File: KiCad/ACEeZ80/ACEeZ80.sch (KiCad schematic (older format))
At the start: 37 parts, among them J1 Connector_Generic:Conn_02x20_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, X2 50MHz

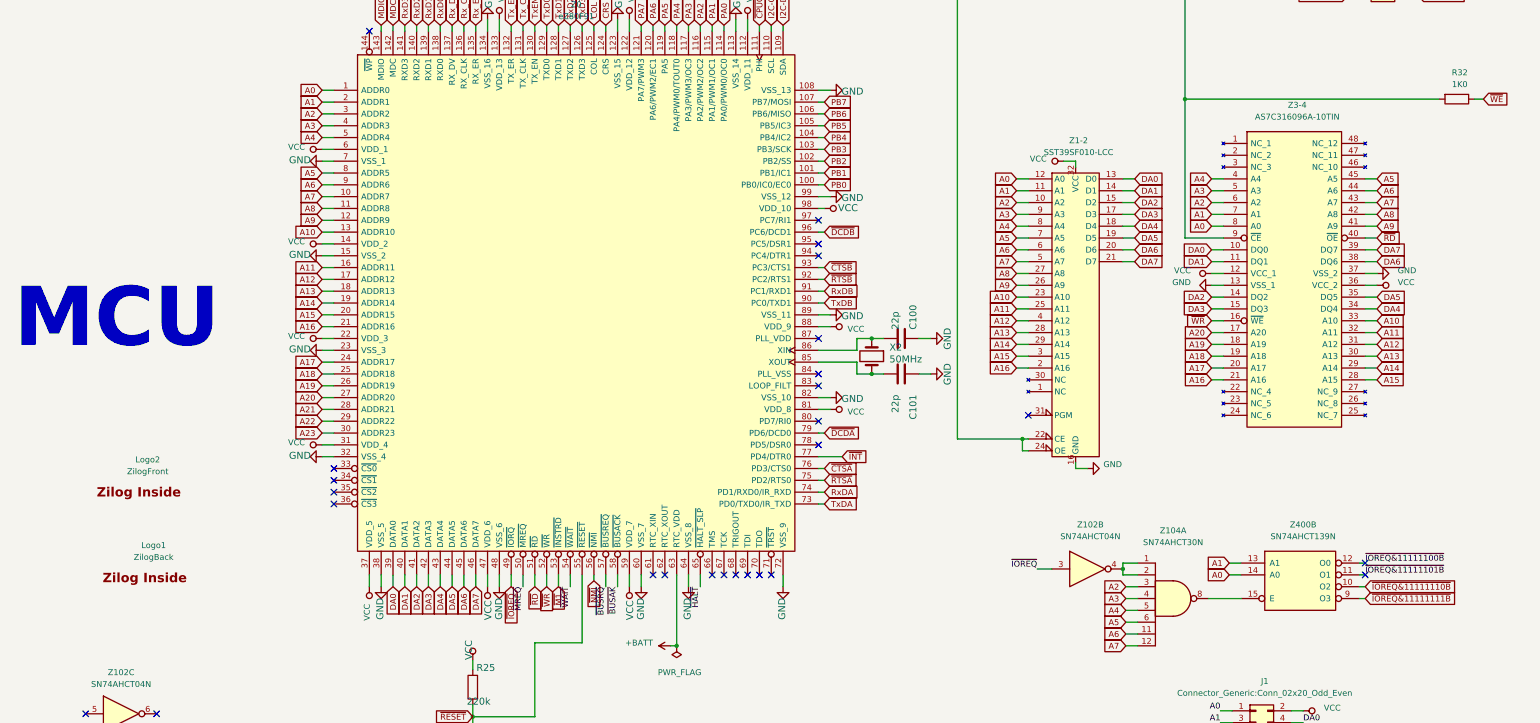
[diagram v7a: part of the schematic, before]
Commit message: Improve EZ80,
Correct fault with layout of EdgeBoard. The test boards physically fitted old ACE add-ons but there was a mistake in the wiring.

Signed-off-by: John Bradley <flypie@rocketmail.com>
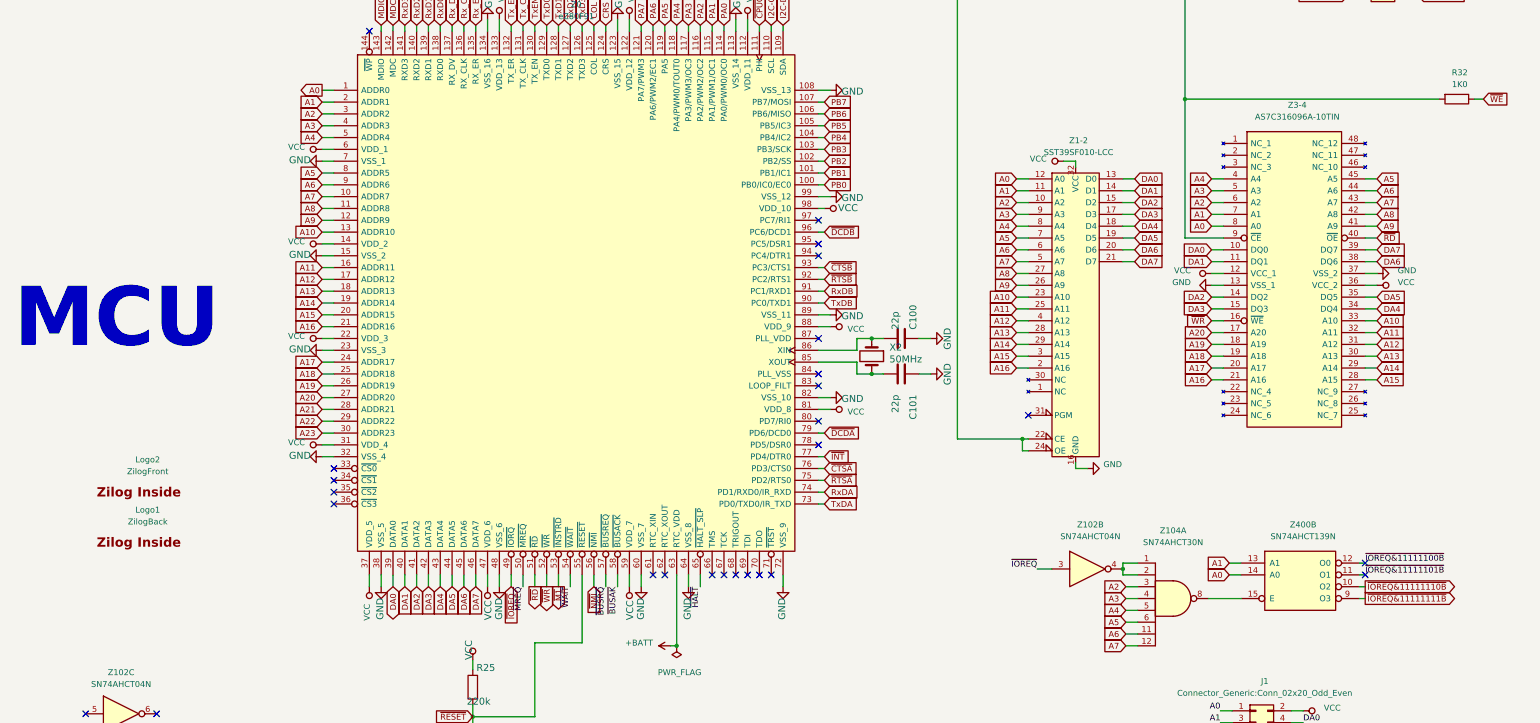
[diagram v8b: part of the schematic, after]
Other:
- moved on the sheet: Logo1
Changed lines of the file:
@@
 L Graphic:ZilogBack Logo1
 U 1 1 5D88DFF8
-P -650 9100
-F 0 "Logo1" H -225 9325 50  0000 C CNN
-F 1 "ZilogBack" H -225 9225 50  0000 C CNN
-F 2 "Symbol:ZilogInsideBack" H -200 9350 50  0001 C CNN
-F 3 "" H -450 9250 50  0001 C CNN
-	1    -650 9100
+P -700 8800
+F 0 "Logo1" H -275 9025 50  0000 C CNN
+F 1 "ZilogBack" H -275 8925 50  0000 C CNN
+F 2 "Symbol:ZilogInsideBack" H -250 9050 50  0001 C CNN
+F 3 "" H -500 8950 50  0001 C CNN
+	1    -700 8800
 	1    0    0    -1
 $EndComp
@@
 Wire Wire Line
 	1300 5625 1200 5625
-Text GLabel 3500 9175 3    50   Input ~ 0
+Text GLabel 3500 9225 3    50   Input ~ 0
 ~NMI
 $Comp
@@
 Wire Wire Line
 	8100 9225 8000 9225
-Text GLabel 10025 9225 2    50   Input ~ 0
+Text GLabel 10025 9225 2    50   Output ~ 0
 ~IOREQ&11111110B
 Wire Wire Line
@@
 Wire Wire Line
 	9975 9325 10025 9325
-Text GLabel 10025 9325 2    50   Input ~ 0
+Text GLabel 10025 9325 2    50   Output ~ 0
 ~IOREQ&11111111B
 Wire Wire Line
@@
 Wire Wire Line
 	1300 5525 1200 5525
-Text GLabel 3200 9225 3    50   Input ~ 0
+Text GLabel 3200 9225 3    50   Output ~ 0
 ~M1
 Wire Wire Line
 	3200 9125 3200 9225
 Wire Wire Line
-	3500 9125 3500 9175
+	3500 9125 3500 9225
 $Comp
 L 74xx:74HCT04 Z102
@@
 Text GLabel 4675 3225 0    50   Input ~ 0
 A12
-Text GLabel 1200 5025 0    50   Input ~ 0
+Text GLabel 1200 5025 0    50   Output ~ 0
 A0
 Text GLabel 1200 5125 0    50   Input ~ 0
@@
 Text GLabel 2800 9225 3    50   Input ~ 0
 ~IOREQ
-Text GLabel 3100 9225 3    50   Input ~ 0
+Text GLabel 3100 9225 3    50   Output ~ 0
 ~WR
-Text GLabel 3000 9225 3    50   Input ~ 0
+Text GLabel 3000 9225 3    50   Output ~ 0
 ~RD
 Text GLabel 9800 1375 0    50   Input ~ 0
@@
 Text GLabel 1900 9225 3    50   Input ~ 0
 DA1
-Text GLabel 1800 9225 3    50   Input ~ 0
+Text GLabel 1800 9225 3    50   BiDi ~ 0
 DA0
 $Comp
@@
 Text GLabel 10500 3275 2    50   Input ~ 0
 ~INT
-Text GLabel 5600 8125 2    50   Input ~ 0
+Text GLabel 5450 8125 2    50   Input ~ 0
 ~INT
 Wire Wire Line
-	5400 8125 5600 8125
+	5400 8125 5450 8125
 Wire Wire Line
 	3300 9125 3300 9225
